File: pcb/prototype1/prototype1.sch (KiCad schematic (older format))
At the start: 92 parts, among them P1 AAA1 HOT, P2 AAA1 GND, P3 AAA2 GND, P4 AAA2 HOT, P5 USB_B, SW1 SPST, SW2 Button, SW3 Button, SW4 Button, SW5 Button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

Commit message: Workin on pcb!
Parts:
- P1, P2, P3, P4: footprint (none) -> spin:test_pin
- SW1: footprint (none) -> Buttons_Switches_ThroughHole:SW_DIP_x1_Slide
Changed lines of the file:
@@
 F 0 "P1" H 3600 7050 50  0000 C CNN
 F 1 "AAA1 HOT" V 3700 6950 50  0000 C CNN
-F 2 "" H 3600 6950 50  0001 C CNN
+F 2 "spin:test_pin" H 3600 6950 50  0001 C CNN
 F 3 "" H 3600 6950 50  0000 C CNN
 	1    3600 6950
@@
 F 0 "P2" H 3600 7350 50  0000 C CNN
 F 1 "AAA1 GND" V 3700 7250 50  0000 C CNN
-F 2 "" H 3600 7250 50  0001 C CNN
+F 2 "spin:test_pin" H 3600 7250 50  0001 C CNN
 F 3 "" H 3600 7250 50  0000 C CNN
 	1    3600 7250
@@
 F 0 "P3" H 4050 7050 50  0000 C CNN
 F 1 "AAA2 GND" V 4150 6950 50  0000 C CNN
-F 2 "" H 4050 6950 50  0001 C CNN
+F 2 "spin:test_pin" H 4050 6950 50  0001 C CNN
 F 3 "" H 4050 6950 50  0000 C CNN
 	1    4050 6950
@@
 F 0 "P4" H 4050 7350 50  0000 C CNN
 F 1 "AAA2 HOT" V 4150 7250 50  0000 C CNN
-F 2 "" H 4050 7250 50  0001 C CNN
+F 2 "spin:test_pin" H 4050 7250 50  0001 C CNN
 F 3 "" H 4050 7250 50  0000 C CNN
 	1    4050 7250
@@
 F 0 "SW1" H 4550 7550 50  0000 C CNN
 F 1 "SPST" H 4550 7350 50  0000 C CNN
-F 2 "" H 4550 7450 50  0001 C CNN
+F 2 "Buttons_Switches_ThroughHole:SW_DIP_x1_Slide" H 4550 7450 50  0001 C CNN
 F 3 "http://www.mouser.com/ds/2/60/-604428.pdf" H 4550 7450 50  0001 C CNN
 F 4 "OS102011MA1QN1C" H 4550 7450 60  0001 C CNN "manf#"

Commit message: pcb stuff
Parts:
- added H1, H2, H3, H4, H5, H6: Hole, spin:Hole-3mm, symbol Hole
- SW1: footprint Buttons_Switches_ThroughHole:SW_DIP_x1_Slide -> spin:EVP-AYG0BA; manf# OS102011MA1QN1C -> EVP-AYG0BA
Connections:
- net GND: now also H1.1, H2.1, H3.1, H4.1, H5.1, H6.1
- net at P4.1 (P1), SW1.1: now also C23.2, L1.2, U6.5 (VIN)
- new net: SW1.2, U6.8 (EN)
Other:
- note added: "Mounting holes"
- note added: "String holes"
- note removed: "CHANGE SWITCH / DO FOOTPRINT"
- moved on the sheet: SW1

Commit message: Connected many things on pcb
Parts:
- U11: footprint TO_SOT_Packages_SMD:SOT-223 -> spin:SOT-223
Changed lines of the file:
@@
 F 0 "U11" H 10400 5500 50  0000 C CNN
 F 1 "LD1117S33CTR" H 10400 4800 50  0000 C CNN
-F 2 "TO_SOT_Packages_SMD:SOT-223" H 10400 5400 50  0001 C CNN
+F 2 "spin:SOT-223" H 10400 5400 50  0001 C CNN
 F 3 "http://www.mouser.com/ds/2/389/CD00000544-310772.pdf" H 10400 5300 50  0001 C CNN
 F 4 "LD1117S33CTR" H 10400 5300 60  0001 C CNN "manf#"

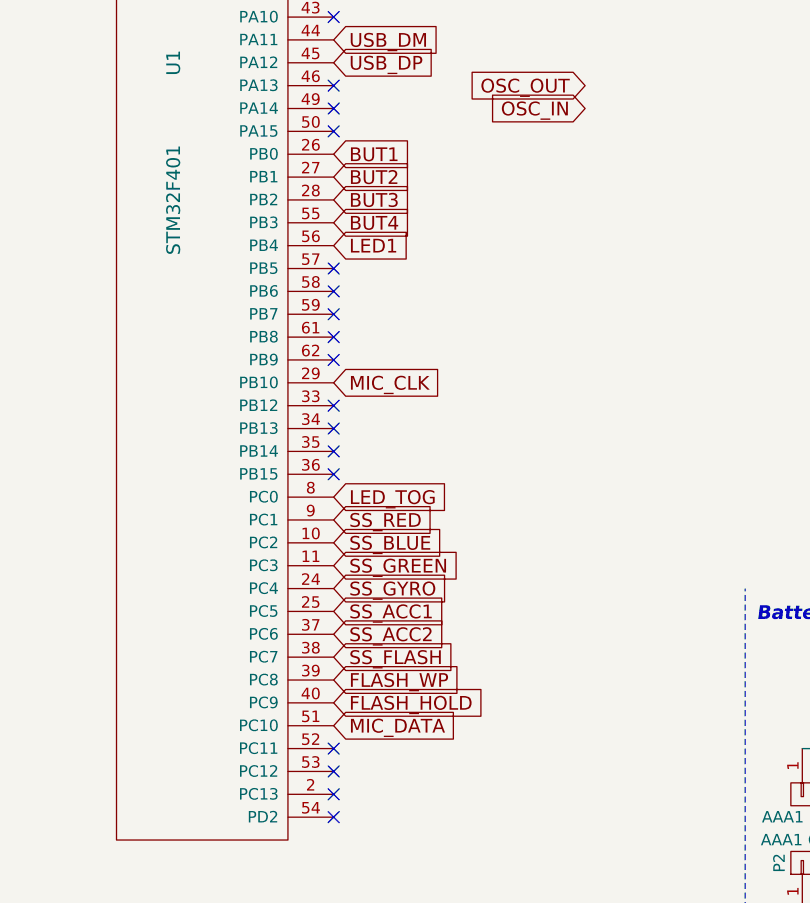
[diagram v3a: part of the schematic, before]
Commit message: swap a couple pins on stm32
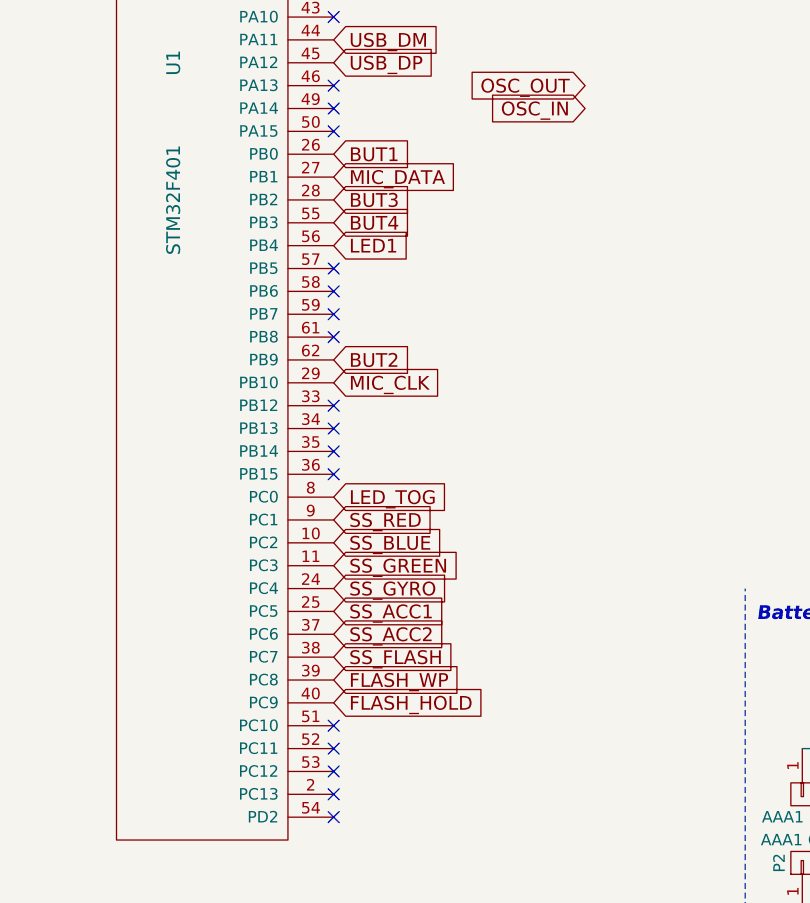
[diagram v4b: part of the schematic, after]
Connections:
- net BUT2: now also U1.62 (PB9); no longer U1.27 (PB1)
- net MIC_DATA: now also U1.27 (PB1); no longer U1.51 (PC10)
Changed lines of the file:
@@
 NoConn ~ 1550 4850
 NoConn ~ 1550 4950
-NoConn ~ 1550 5050
 NoConn ~ 1550 5250
 NoConn ~ 1550 5350
@@
 Text GLabel 1550 4150 2    60   Input ~ 0
 BUT1
-Text GLabel 1550 4250 2    60   Input ~ 0
+Text GLabel 1550 5050 2    60   Input ~ 0
 BUT2
 Text GLabel 1550 4350 2    60   Input ~ 0
@@
 Text GLabel 1550 5150 2    60   Input ~ 0
 MIC_CLK
-Text GLabel 1550 6650 2    60   Input ~ 0
+Text GLabel 1550 4250 2    60   Input ~ 0
 MIC_DATA
 Text GLabel 3500 2400 2    60   Input ~ 0
@@
 Wire Notes Line
 	10500 6500 10500 5900
+NoConn ~ 1550 6650
 $EndSCHEMATC

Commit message: pcb is connected!
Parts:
- removed SW2, SW3, SW4, SW5: Button, spin:Button, symbol SW_PUSH
- added H10, H7, H8, H9: Hole, spin:Zip-tie-slot, symbol Hole
- added SW2, SW3, SW4, SW5: SPST_two_terminals, spin:Button, symbol SPST_two_terminals
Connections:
- net +3V3: now also R3.1, R4.1; no longer R3.2, R4.2
- net BOOT0: now also SW2.2; no longer R3.1, U1.26 (PB0)
- net BUT2: now also R4.2, SW3.1; no longer R4.1
- net BUT3: now also SW4.1
- net BUT4: now also SW5.1; no longer R6.1
- net GND: now also H10.1, H7.1, H8.1, H9.1, SW2.3, SW2.4, SW3.3, SW3.4, SW4.3, SW4.4, SW5.3, SW5.4
- new net: R6.1, SW5.2
- new net BUT1: R3.2, SW2.1, U1.26 (PB0)
- no-connect marks 33 -> 35
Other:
- note added: "Zip-tie slots"
- moved on the sheet: C18, C19, C20, C21, C23, L1, P1, P2, P3, P4, R1, R2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

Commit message: Finish prototype1!!!
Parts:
- added C26: 10n, Capacitors_SMD:C_0805_HandSoldering, symbol C
- added U12: ASDMB-12.000MHZ-LC-T, spin:ASDMB-12.000MHZ-LC-T, symbol ASDMB-12.000MHZ-LC-T
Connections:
- net +3V3: now also C26.1, U12.4 (Vdd)
- net GND: now also C26.2, U12.2 (GND)
- net OSC_IN: now also U12.3 (Output)
- net OSC_OUT: no longer names the net of U1.6 (PH1_-_OSC_OUT)
- no-connect marks 35 -> 37
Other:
- note removed: "ADD:\nCrystal"
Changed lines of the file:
@@
 U 1 1 575D9F93
 P 6400 6850
-F 0 "L1" V 6300 6850 50  0000 C CNN
-F 1 "1uH 4.9mOhm" V 6500 6850 50  0000 C CNN
+F 0 "L1" V 6500 6850 50  0000 C CNN
+F 1 "1uH 4.9mOhm" V 6350 6850 50  0000 C CNN
 F 2 "spin:SRU1028-10x10-Octogon" H 6400 6850 50  0001 C CNN
 F 3 "http://www.mouser.com/ds/2/54/RU1028-778233.pdf" H 6400 6850 50  0001 C CNN
@@
 	1    0    0    -1
 $EndComp
-Text Notes -800 5150 0    60   ~ 0
-ADD:\nCrystal
 $Comp
 L +3.3V #PWR020
@@
 Text GLabel 1550 2150 2    60   Input ~ 0
 OSC_IN
-Text GLabel 1550 2250 2    60   Input ~ 0
-OSC_OUT
 Text Notes 7300 650  0    60   Italic 12
 LED Drivers
@@
 Batteries
 NoConn ~ 1550 2350
-Text GLabel 2650 3950 0    60   Input ~ 0
+Text GLabel 2650 3550 1    60   Input ~ 0
 OSC_IN
-Text GLabel 2650 3850 0    60   Input ~ 0
-OSC_OUT
 Text GLabel 1550 5150 2    60   Input ~ 0
 MIC_CLK
@@
 Text Notes 3200 2850 0    60   ~ 0
 Caps near pin 1!
-Text Notes 2800 3350 0    60   Italic 12
+Text Notes 2950 3300 0    60   Italic 12
 Crystal
 $Comp
@@
 	3500 550  3500 1950
 Wire Notes Line
-	6450 4700 4050 4700
-Wire Notes Line
 	4050 1950 4050 6350
 Wire Wire Line
@@
 Wire Wire Line
 	6100 7400 6100 7000
-Wire Wire Line
-	5100 7400 5100 7550
 Connection ~ 5100 7550
 Text Notes 10600 6000 0    60   Italic 12
@@
 Connection ~ 10000 6050
 Connection ~ 10300 6050
+$Comp
+L GND #PWR056
+U 1 1 578D6714
+P 2650 3750
+F 0 "#PWR056" H 2650 3500 50  0001 C CNN
+F 1 "GND" H 2650 3600 50  0000 C CNN
+F 2 "" H 2650 3750 50  0000 C CNN
+F 3 "" H 2650 3750 50  0000 C CNN
+	1    2650 3750
+	1    0    0    -1
+$EndComp
+NoConn ~ 1550 2250
+$Comp
+L ASDMB-12.000MHZ-LC-T U12
+U 1 1 578DFC0C
+P 3100 3600
+F 0 "U12" H 3100 3750 60  0000 C CNN
+F 1 "ASDMB-12.000MHZ-LC-T" H 3350 3400 60  0000 C CNN
+F 2 "spin:ASDMB-12.000MHZ-LC-T" H 3000 3850 60  0001 C CNN
+F 3 "http://www.mouser.com/ds/2/3/ASDMB-29928.pdf" H 3100 3100 60  0001 C CNN
+F 4 "ASDMB-12.000MHZ-LC-T" H 3100 3200 60  0001 C CNN "manf#"
+	1    3100 3600
+	1    0    0    -1
+$EndComp
+NoConn ~ 3600 3650
+$Comp
+L +3.3V #PWR057
+U 1 1 578E032D
+P 3600 3450
+F 0 "#PWR057" H 3600 3300 50  0001 C CNN
+F 1 "+3.3V" H 3600 3590 50  0000 C CNN
+F 2 "" H 3600 3450 50  0000 C CNN
+F 3 "" H 3600 3450 50  0000 C CNN
+	1    3600 3450
+	1    0    0    -1
+$EndComp
+Wire Wire Line
+	3600 3450 3600 3550
+Wire Wire Line
+	3800 3750 2650 3750
+Wire Wire Line
+	2650 3750 2650 3650
+Connection ~ 2650 3750
+Wire Wire Line
+	3800 3450 3600 3450
+Connection ~ 3600 3450
+Wire Notes Line
+	2500 3150 2500 4000
+Wire Notes Line
+	2500 4000 4050 4000
+$Comp
+L C C26
+U 1 1 578E5B6F
+P 3800 3600
+F 0 "C26" H 3825 3700 50  0000 L CNN
+F 1 "10n" H 3825 3500 50  0000 L CNN
+F 2 "Capacitors_SMD:C_0805_HandSoldering" H 3838 3450 50  0001 C CNN
+F 3 "http://www.mouser.com/ds/2/447/UPY-GPHC_X7R_6.3V-to-50V-v12-709413.pdf" H 3800 3600 50  0001 C CNN
+F 4 "CC0805JRX7R0BB103" H 3800 3600 60  0001 C CNN "manf#"
+	1    3800 3600
+	1    0    0    -1
+$EndComp
+Wire Wire Line
+	5100 7550 5100 7400
 $EndSCHEMATC
